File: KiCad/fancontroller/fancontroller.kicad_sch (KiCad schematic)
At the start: 0 parts

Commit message: feat: place recovered component symbols and values for BOM traceability
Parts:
- added C1: 560pF, Capacitor_SMD:C_1206_3216Metric, symbol Device:C
- added C2, C3: 100nF, Capacitor_SMD:C_0603_1608Metric, symbol Device:C
- added C4: 100pF, Capacitor_SMD:C_1206_3216Metric, symbol Device:C
- added C5: 47uF 10V, Capacitor_SMD:CP_Elec_6.3x5.8, symbol Device:C_Polarized
- added IC1, IC3: NE555DR, Package_SO:SOIC-8_3.9x4.9mm_P1.27mm, symbol Timer:NE555D
- added IC2: LM311DR, Package_SO:SOIC-8_3.9x4.9mm_P1.27mm, symbol Comparator:LM311
- added J1: Fan 4-pin, symbol Connector_Generic:Conn_01x04
- added J2: Power input, symbol Connector_Generic:Conn_01x02
- added P1: 10k, symbol Device:R_Potentiometer
- added R1: 10k, Resistor_SMD:R_1206_3216Metric, symbol Device:R
- added R2: 47k, Resistor_SMD:R_1206_3216Metric, symbol Device:R
- added R3, R4: 9.1k, Resistor_SMD:R_1206_3216Metric, symbol Device:R
- added R5: 1k, Resistor_SMD:R_1206_3216Metric, symbol Device:R

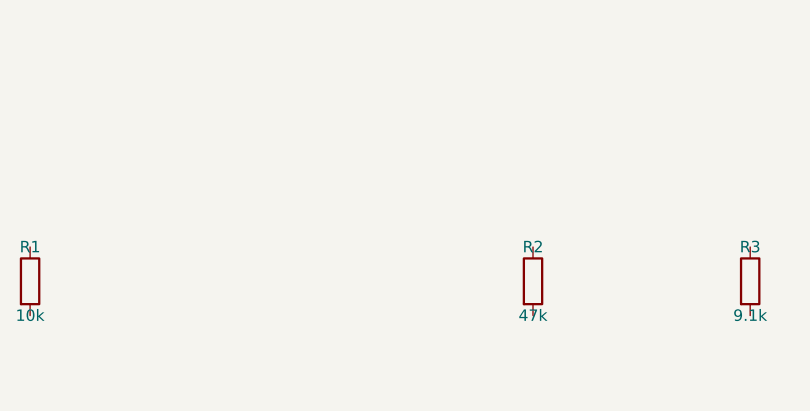
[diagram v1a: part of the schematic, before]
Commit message: feat: populate sourced BOM and document KiCad reconstruction
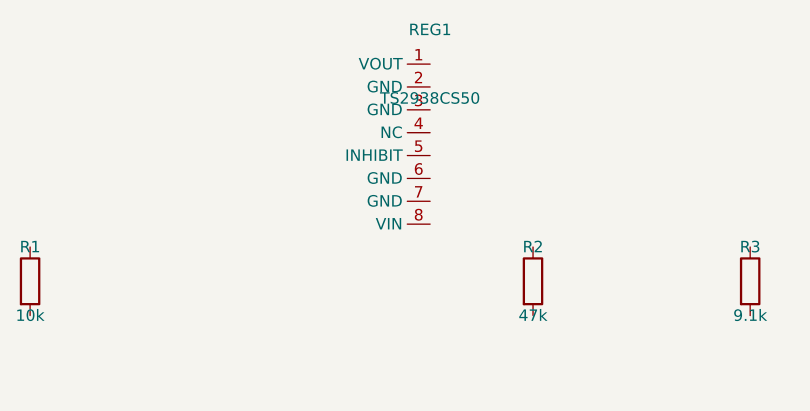
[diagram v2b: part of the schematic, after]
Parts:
- added REG1: TS2938CS50, Package_SO:SOIC-8_3.9x4.9mm_P1.27mm, symbol custom_symbols:TS2938CS50
- C1: LCSC (none) -> C2178336; MPN (none) -> C1206C561K5RAC7800
- C2, C3: LCSC (none) -> C2167748; MPN (none) -> C0603C104K3RALTU
- C4: LCSC (none) -> C2178961; MPN (none) -> C1206C101KCRACTU
- C5: MPN (none) -> UUL1A470MCL1GS
- IC1, IC3: LCSC (none) -> C7593; MPN (none) -> NE555DR
- IC2: LCSC (none) -> C12597; MPN (none) -> LM311DR
- J1: MPN (none) -> 0470531000
- P1: LCSC (none) -> C6626952; MPN (none) -> PDF241-S425F-103B0
- R1: LCSC (none) -> C132649; MPN (none) -> RC1206FR-0710KL
- R2: LCSC (none) -> C137270; MPN (none) -> RC1206FR-0747KL
- R3, R4: MPN (none) -> RC1206FR-079K1L
- R5: LCSC (none) -> C131398; MPN (none) -> RC1206FR-071KL
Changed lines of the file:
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@@
+			(effects (font (size 1.27 1.27)) (hide yes))
+		)
+		(property "MPN" "NE555DR"
+			(at 59.69 85.09 0)
+			(effects (font (size 1.27 1.27)) (hide yes))
+		)
+		(property "LCSC" "C7593"
+			(at 59.69 85.09 0)
 			(effects (font (size 1.27 1.27)) (hide yes))
 		)
@@
 			(effects (font (size 1.27 1.27)) (hide yes))
 		)
+		(property "MPN" "LM311DR"
+			(at 144.78 85.09 0)
+			(effects (font (size 1.27 1.27)) (hide yes))
+		)
+		(property "LCSC" "C12597"
+			(at 144.78 85.09 0)
+			(effects (font (size 1.27 1.27)) (hide yes))
+		)
 		(instances
 			(project "fancontroller"
@@
 			(effects (font (size 1.27 1.27)) (hide yes))
 		)
+		(property "MPN" "NE555DR"
+			(at 224.79 85.09 0)
+			(effects (font (size 1.27 1.27)) (hide yes))
+		)
+		(property "LCSC" "C7593"
+			(at 224.79 85.09 0)
+			(effects (font (size 1.27 1.27)) (hide yes))
+		)
 		(instances
 			(project "fancontroller"
@@
 			(effects (font (size 1.27 1.27)) (hide yes))
 		)
+		(property "MPN" "C1206C561K5RAC7800"
+			(at 49.53 129.54 0)
+			(effects (font (size 1.27 1.27)) (hide yes))
+		)
+		(property "LCSC" "C2178336"
+			(at 49.53 129.54 0)
+			(effects (font (size 1.27 1.27)) (hide yes))
+		)
 		(instances
 			(project "fancontroller"
@@
 			(effects (font (size 1.27 1.27)) (hide yes))
 		)
+		(property "MPN" "C0603C104K3RALTU"
+			(at 134.62 129.54 0)
+			(effects (font (size 1.27 1.27)) (hide yes))
+		)
+		(property "LCSC" "C2167748"
+			(at 134.62 129.54 0)
+			(effects (font (size 1.27 1.27)) (hide yes))
+		)
 		(instances
 			(project "fancontroller"
@@
 			(effects (font (size 1.27 1.27)) (hide yes))
 		)
+		(property "MPN" "C0603C104K3RALTU"
+			(at 214.63 129.54 0)
+			(effects (font (size 1.27 1.27)) (hide yes))
+		)
+		(property "LCSC" "C2167748"
+			(at 214.63 129.54 0)
+			(effects (font (size 1.27 1.27)) (hide yes))
+		)
 		(instances
 			(project "fancontroller"
@@
 			(effects (font (size 1.27 1.27)) (hide yes))
 		)
+		(property "MPN" "C1206C101KCRACTU"
+			(at 154.94 129.54 0)
+			(effects (font (size 1.27 1.27)) (hide yes))
+		)
+		(property "LCSC" "C2178961"
+			(at 154.94 129.54 0)
+			(effects (font (size 1.27 1.27)) (hide yes))
+		)
 		(instances
 			(project "fancontroller"
@@
 			(effects (font (size 1.27 1.27)) (hide yes))
 		)
+		(property "MPN" "UUL1A470MCL1GS"
+			(at 30.48 129.54 0)
+			(effects (font (size 1.27 1.27)) (hide yes))
+		)
 		(instances
 			(project "fancontroller"
@@
 			(effects (font (size 1.27 1.27)) (hide yes))
 		)
+		(property "MPN" "RC1206FR-0710KL"
+			(at 44.45 54.61 0)
+			(effects (font (size 1.27 1.27)) (hide yes))
+		)
+		(property "LCSC" "C132649"
+			(at 44.45 54.61 0)
+			(effects (font (size 1.27 1.27)) (hide yes))
+		)
 		(instances
 			(project "fancontroller"
@@
 			(effects (font (size 1.27 1.27)) (hide yes))
 		)
+		(property "MPN" "RC1206FR-0747KL"
+			(at 100.33 54.61 0)
+			(effects (font (size 1.27 1.27)) (hide yes))
+		)
+		(property "LCSC" "C137270"
+			(at 100.33 54.61 0)
+			(effects (font (size 1.27 1.27)) (hide yes))
+		)
 		(instances
 			(project "fancontroller"
@@
 			(effects (font (size 1.27 1.27)) (hide yes))
 		)
+		(property "MPN" "RC1206FR-079K1L"
+			(at 124.46 54.61 0)
+			(effects (font (size 1.27 1.27)) (hide yes))
+		)
 		(instances
 			(project "fancontroller"
@@
 			(effects (font (size 1.27 1.27)) (hide yes))
 		)
+		(property "MPN" "RC1206FR-079K1L"
+			(at 165.1 54.61 0)
+			(effects (font (size 1.27 1.27)) (hide yes))
+		)
 		(instances
 			(project "fancontroller"
@@
 			(effects (font (size 1.27 1.27)) (hide yes))
 		)
+		(property "MPN" "RC1206FR-071KL"
+			(at 204.47 54.61 0)
+			(effects (font (size 1.27 1.27)) (hide yes))
+		)
+		(property "LCSC" "C131398"
+			(at 204.47 54.61 0)
+			(effects (font (size 1.27 1.27)) (hide yes))
+		)
 		(instances
 			(project "fancontroller"
@@
 			(effects (font (size 1.27 1.27)) (hide yes))
 		)
+		(property "MPN" "PDF241-S425F-103B0"
+			(at 124.46 100.33 0)
+			(effects (font (size 1.27 1.27)) (hide yes))
+		)
+		(property "LCSC" "C6626952"
+			(at 124.46 100.33 0)
+			(effects (font (size 1.27 1.27)) (hide yes))
+		)
 		(instances
 			(project "fancontroller"
@@
 			(effects (font (size 1.27 1.27)) (hide yes))
 		)
+		(property "MPN" "0470531000"
+			(at 265.43 64.77 0)
+			(effects (font (size 1.27 1.27)) (hide yes))
+		)
 		(instances
 			(project "fancontroller"
@@
 				)
 			)
+		)
+	)
+	(symbol
+		(lib_id "custom_symbols:TS2938CS50")
+		(at 88.9 30.48 0)
+		(unit 1)
+		(exclude_from_sim no)
+		(in_bom yes)
+		(on_board yes)
+		(dnp no)
+		(property "Reference" "REG1"
+			(at 88.9 26.67 0)
+			(effects (font (size 1.27 1.27)))
+		)
+		(property "Value" "TS2938CS50"
+			(at 88.9 34.29 0)
+			(effects (font (size 1.27 1.27)))
+		)
+		(property "Footprint" "Package_SO:SOIC-8_3.9x4.9mm_P1.27mm"
+			(at 88.9 30.48 0)
+			(effects (font (size 1.27 1.27)) (hide yes))
+		)
+		(property "Datasheet" "~"
+			(at 88.9 30.48 0)
+			(effects (font (size 1.27 1.27)) (hide yes))
+		)
+		(property "MPN" "TS2938CS50 RLG"
+			(at 88.9 30.48 0)
+			(effects (font (size 1.27 1.27)) (hide yes))
+		)
+		(property "LCSC" "C557546"
+			(at 88.9 30.48 0)
+			(effects (font (size 1.27 1.27)) (hide yes))
+		)
+		(instances
+			(project "fancontroller"
+				(path "/97550efb-8a25-4e8f-a675-896628ec4139"
+					(reference "REG1") (unit 1)
+				)
+			)

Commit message: feat: recover original footprints and correct pad placement geometry
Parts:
- C1, C4: footprint Capacitor_SMD:C_1206_3216Metric -> Recovered2018:C_1206_3216Metric_Pad1.42x1.75mm_HandSolder
- C2, C3: footprint Capacitor_SMD:C_0603_1608Metric -> Recovered2018:C_0603_1608Metric_Pad1.05x0.95mm_HandSolder
- C5: footprint Capacitor_SMD:CP_Elec_6.3x5.8 -> Recovered2018:CP_Elec_6.3x5.8
- IC1, IC2, IC3, REG1: footprint Package_SO:SOIC-8_3.9x4.9mm_P1.27mm -> Recovered2018:SOIC-8_3.9x4.9mm_P1.27mm
- R1, R2, R3, R4, R5: footprint Resistor_SMD:R_1206_3216Metric -> Recovered2018:R_1206_3216Metric_Pad1.42x1.75mm_HandSolder
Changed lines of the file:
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@@
 			(effects (font (size 1.27 1.27)))
 		)
-		(property "Footprint" "Package_SO:SOIC-8_3.9x4.9mm_P1.27mm"
+		(property "Footprint" "Recovered2018:SOIC-8_3.9x4.9mm_P1.27mm"
 			(at 59.69 85.09 0)
 			(effects (font (size 1.27 1.27)) (hide yes))
@@
 			(effects (font (size 1.27 1.27)))
 		)
-		(property "Footprint" "Package_SO:SOIC-8_3.9x4.9mm_P1.27mm"
+		(property "Footprint" "Recovered2018:SOIC-8_3.9x4.9mm_P1.27mm"
 			(at 144.78 85.09 0)
 			(effects (font (size 1.27 1.27)) (hide yes))
@@
 			(effects (font (size 1.27 1.27)))
 		)
-		(property "Footprint" "Package_SO:SOIC-8_3.9x4.9mm_P1.27mm"
+		(property "Footprint" "Recovered2018:SOIC-8_3.9x4.9mm_P1.27mm"
 			(at 224.79 85.09 0)
 			(effects (font (size 1.27 1.27)) (hide yes))
@@
 			(effects (font (size 1.27 1.27)))
 		)
-		(property "Footprint" "Capacitor_SMD:C_1206_3216Metric"
+		(property "Footprint" "Recovered2018:C_1206_3216Metric_Pad1.42x1.75mm_HandSolder"
 			(at 49.53 129.54 0)
 			(effects (font (size 1.27 1.27)) (hide yes))
@@
 			(effects (font (size 1.27 1.27)))
 		)
-		(property "Footprint" "Capacitor_SMD:C_0603_1608Metric"
+		(property "Footprint" "Recovered2018:C_0603_1608Metric_Pad1.05x0.95mm_HandSolder"
 			(at 134.62 129.54 0)
 			(effects (font (size 1.27 1.27)) (hide yes))
@@
 			(effects (font (size 1.27 1.27)))
 		)
-		(property "Footprint" "Capacitor_SMD:C_0603_1608Metric"
+		(property "Footprint" "Recovered2018:C_0603_1608Metric_Pad1.05x0.95mm_HandSolder"
 			(at 214.63 129.54 0)
 			(effects (font (size 1.27 1.27)) (hide yes))
@@
 			(effects (font (size 1.27 1.27)))
 		)
-		(property "Footprint" "Capacitor_SMD:C_1206_3216Metric"
+		(property "Footprint" "Recovered2018:C_1206_3216Metric_Pad1.42x1.75mm_HandSolder"
 			(at 154.94 129.54 0)
 			(effects (font (size 1.27 1.27)) (hide yes))
@@
 			(effects (font (size 1.27 1.27)))
 		)
-		(property "Footprint" "Capacitor_SMD:CP_Elec_6.3x5.8"
+		(property "Footprint" "Recovered2018:CP_Elec_6.3x5.8"
 			(at 30.48 129.54 0)
 			(effects (font (size 1.27 1.27)) (hide yes))
@@
 			(effects (font (size 1.27 1.27)))
 		)
-		(property "Footprint" "Resistor_SMD:R_1206_3216Metric"
+		(property "Footprint" "Recovered2018:R_1206_3216Metric_Pad1.42x1.75mm_HandSolder"
 			(at 44.45 54.61 0)
 			(effects (font (size 1.27 1.27)) (hide yes))
@@
 			(effects (font (size 1.27 1.27)))
 		)
-		(property "Footprint" "Resistor_SMD:R_1206_3216Metric"
+		(property "Footprint" "Recovered2018:R_1206_3216Metric_Pad1.42x1.75mm_HandSolder"
 			(at 100.33 54.61 0)
 			(effects (font (size 1.27 1.27)) (hide yes))
@@
 			(effects (font (size 1.27 1.27)))
 		)
-		(property "Footprint" "Resistor_SMD:R_1206_3216Metric"
+		(property "Footprint" "Recovered2018:R_1206_3216Metric_Pad1.42x1.75mm_HandSolder"
 			(at 124.46 54.61 0)
 			(effects (font (size 1.27 1.27)) (hide yes))
@@
 			(effects (font (size 1.27 1.27)))
 		)
-		(property "Footprint" "Resistor_SMD:R_1206_3216Metric"
+		(property "Footprint" "Recovered2018:R_1206_3216Metric_Pad1.42x1.75mm_HandSolder"
 			(at 165.1 54.61 0)
 			(effects (font (size 1.27 1.27)) (hide yes))
@@
 			(effects (font (size 1.27 1.27)))
 		)
-		(property "Footprint" "Resistor_SMD:R_1206_3216Metric"
+		(property "Footprint" "Recovered2018:R_1206_3216Metric_Pad1.42x1.75mm_HandSolder"
 			(at 204.47 54.61 0)
 			(effects (font (size 1.27 1.27)) (hide yes))
@@
 			(effects (font (size 1.27 1.27)))
 		)
-		(property "Footprint" "Package_SO:SOIC-8_3.9x4.9mm_P1.27mm"
+		(property "Footprint" "Recovered2018:SOIC-8_3.9x4.9mm_P1.27mm"
 			(at 88.9 30.48 0)
 			(effects (font (size 1.27 1.27)) (hide yes))

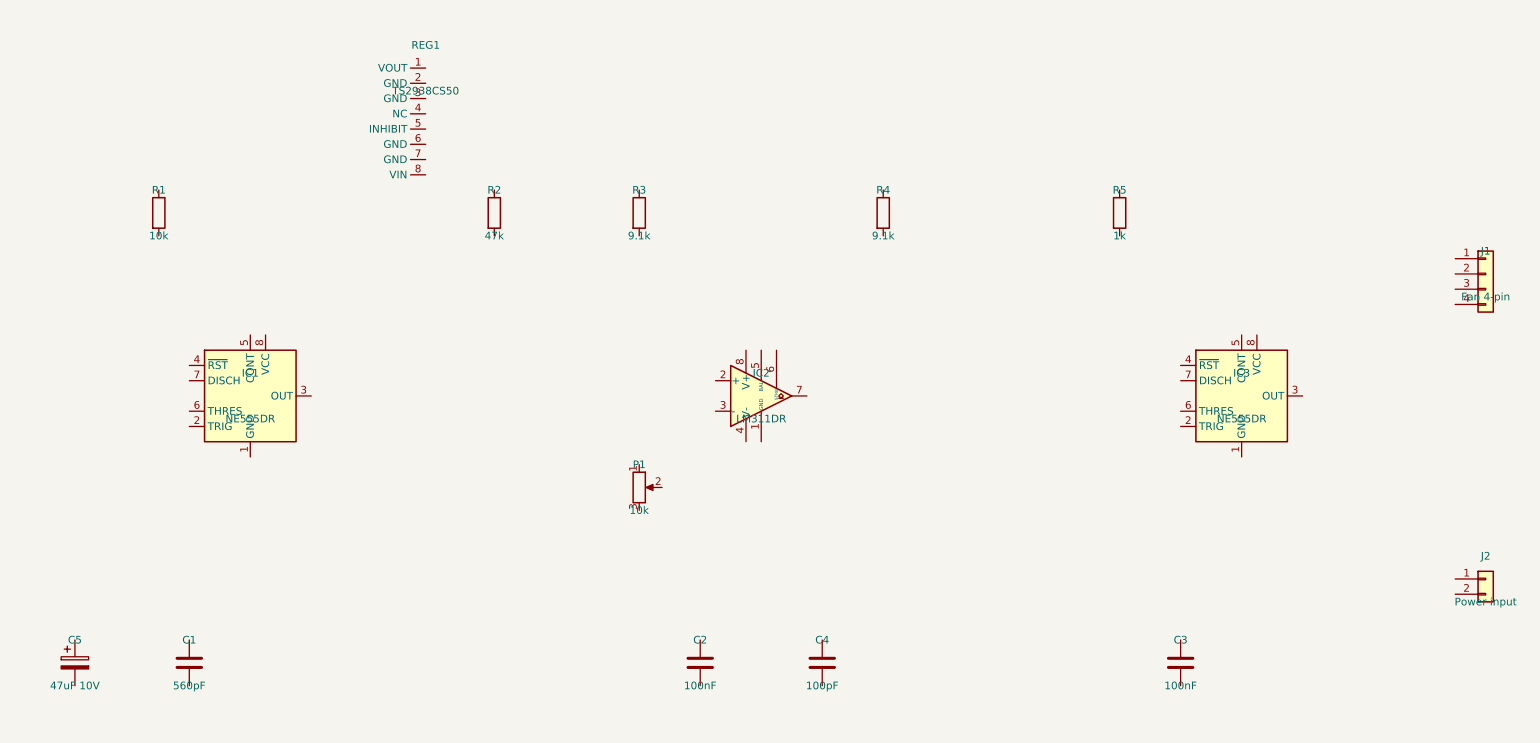
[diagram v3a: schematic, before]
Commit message: feat: reconstruct fan controller schematic connections and clear ERC
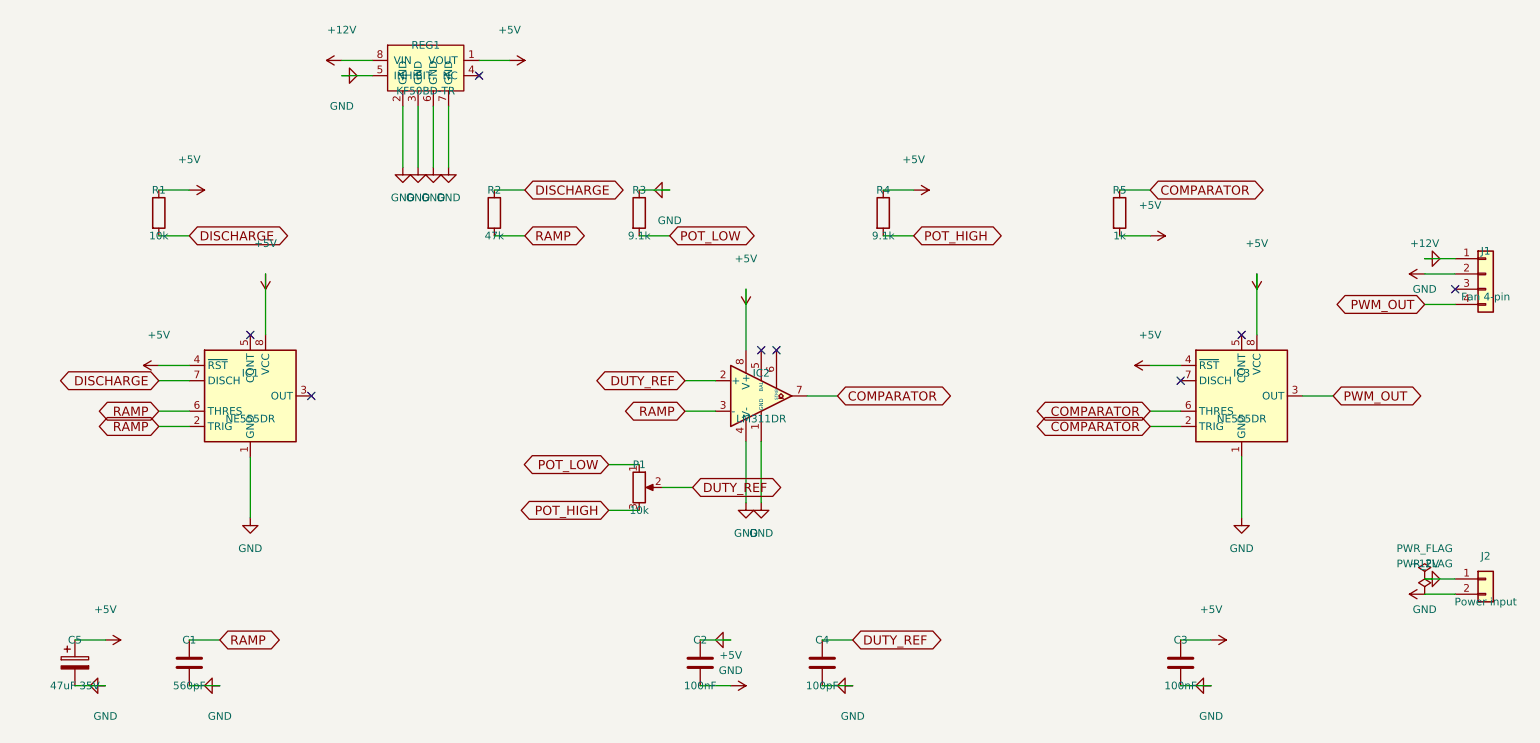
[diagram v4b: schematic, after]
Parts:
- removed REG1: TS2938CS50, Recovered2018:SOIC-8_3.9x4.9mm_P1.27mm, symbol custom_symbols:TS2938CS50
- added REG1: KF50BD-TR, Recovered2018:SOIC-8_3.9x4.9mm_P1.27mm, symbol custom_symbols:KF50BD_TR
- C1: LCSC C2178336 -> C577166; MPN C1206C561K5RAC7800 -> CC1206JRNPO9BN561
- C4: LCSC C2178961 -> C113888; MPN C1206C101KCRACTU -> CC1206JRNPOBBN101
- C5: value 47uF 10V -> 47uF 35V; LCSC (none) -> C336786; MPN UUL1A470MCL1GS -> EEEFK1V470AP
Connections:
- net GND: now reaches C2.1
- net GND: now also C1.2, C3.2, C4.2, C5.2, IC1.1 (GND), IC2.1 (GND), IC2.4 (V-), IC3.1 (GND), J1.1 (Pin_1), J2.1 (Pin_1), R3.1, REG1.2 (GND), REG1.3 (GND), REG1.5 (INHIBIT), REG1.6 (GND), REG1.7 (GND)
- net +5V: now reaches C2.2
- net +5V: now also C3.1, C5.1, IC1.4 (~{RST}), IC1.8 (VCC), IC2.8 (V+), IC3.4 (~{RST}), IC3.8 (VCC), R1.1, R4.1, R5.2, REG1.1 (VOUT)
- net DISCHARGE: now reaches R1.2
- net DISCHARGE: now also IC1.7 (DISCH), R2.1
- net COMPARATOR: now reaches R5.1
- net COMPARATOR: now also IC2.7, IC3.2 (TRIG), IC3.6 (THRES)
- net POT_LOW: now reaches R3.2
- net POT_LOW: now also P1.1
- net DUTY_REF: now reaches P1.2
- net DUTY_REF: now also C4.1, IC2.2 (+)
- net POT_HIGH: now reaches P1.3
- net POT_HIGH: now also R4.2
- net PWM_OUT: now reaches IC3.3 (OUT)
- net PWM_OUT: now also J1.4 (Pin_4)
- net RAMP: now reaches R2.2
- net RAMP: now also C1.1, IC1.2 (TRIG), IC1.6 (THRES), IC2.3 (-)
- net +12V: now reaches J2.2 (Pin_2)
- net +12V: now also J1.2 (Pin_2), REG1.8 (VIN)
- no-connect marks 0 -> 8
